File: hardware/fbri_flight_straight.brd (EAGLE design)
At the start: 12 x 55 mm, 38 parts, among them U1 SAM_D20E, U2 SI4060, U3 MAX1947, U4 ANTENOVA_GPS_M10382, U5 S25FS-S

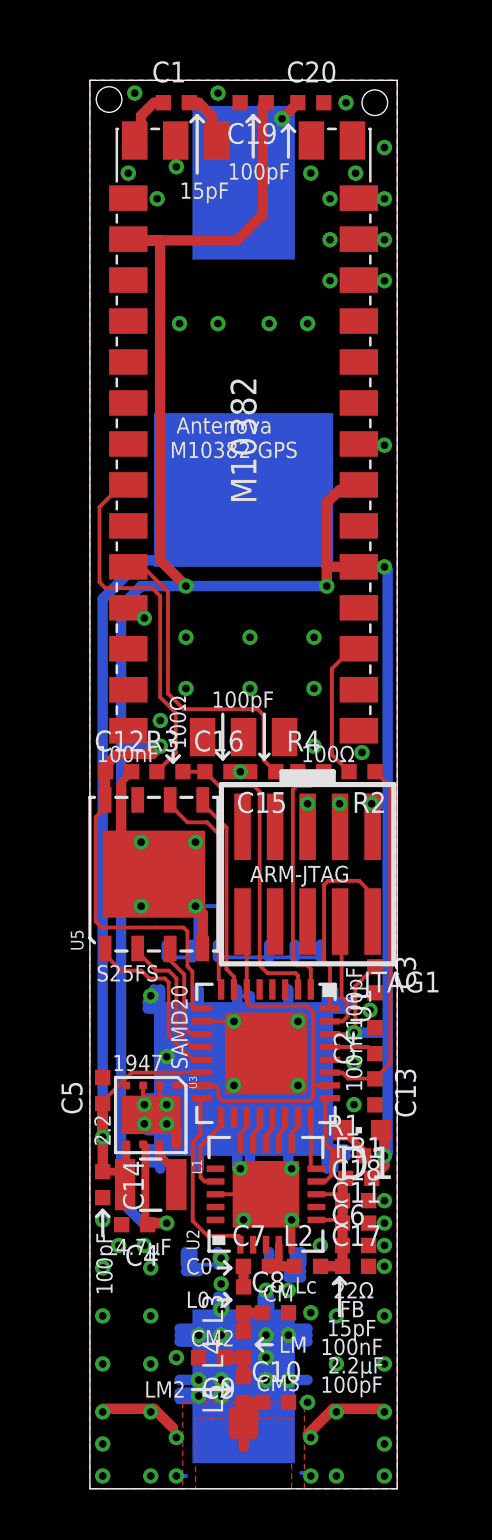
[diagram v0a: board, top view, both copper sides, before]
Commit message: Nearly there, about to re-work MAX1947
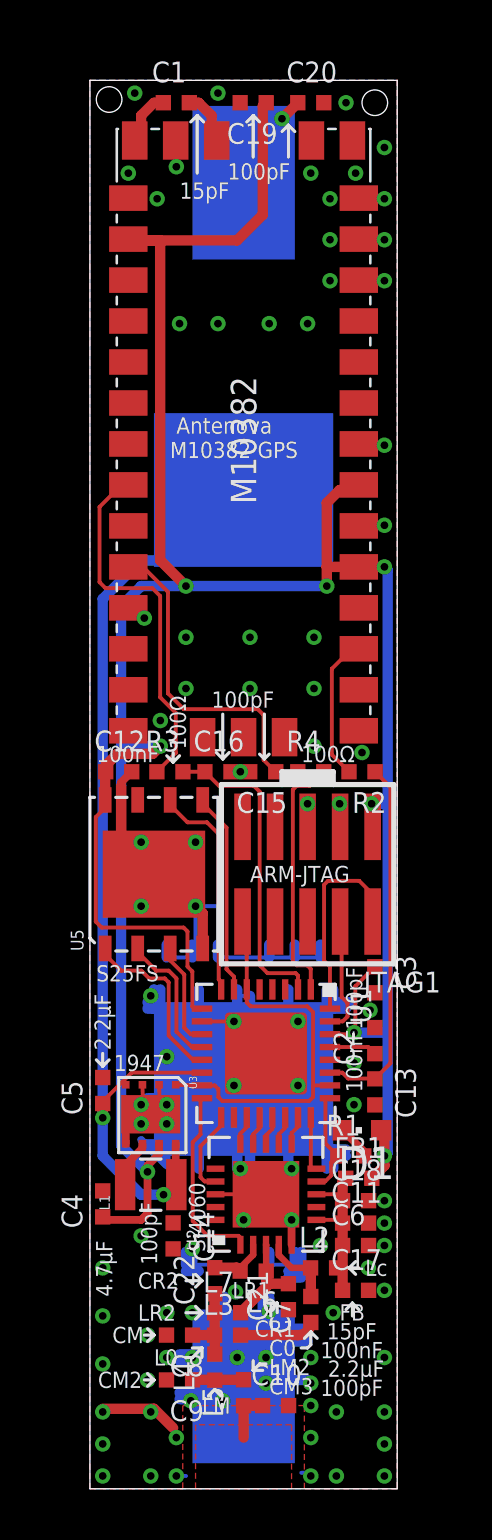
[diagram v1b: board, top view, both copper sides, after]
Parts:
- added C21: 15pF, microbuilder_v3:_0402
- added C22, L6, L7: DNP, microbuilder_v3:_0402
- moved C8 3.85 mm to (3.50, 6.00), turned to 180 degrees
- moved C14 3.40 mm to (3.25, 9.88)
- moved C7 2.71 mm to (8.62, 7.00), turned to 90 degrees
- moved C9 1.53 mm to (3.50, 4.25)
- moved L3 1.51 mm to (5.38, 6.00), turned to 0 degrees
- moved C4 1.49 mm to (0.50, 11.1), turned to 90 degrees
- moved L4 1.43 mm to (4.88, 4.75)
- moved C17 0.94 mm to (10.4, 7.75)
- moved L2 0.63 mm to (9.12, 8.62)
- moved C10 0.12 mm to (7.25, 3.25)
- moved L5 0.12 mm to (6.00, 3.75)
- turned L1 to 90 degrees
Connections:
- new net RXN: C21.2, L6.1, L7.2, U2.3
- new net RXP: C22.2, L6.2, U2.2
- net 1.2V: now also U3.8; no longer U3.5
- net 1.8V: now also U3.7; no longer U3.6
- net FILTER1: now also C22.1, L7.1
- net GND: now also C21.1, U3.5; no longer U3.8
- net LX: now also U3.6; no longer U3.7
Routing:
- net RXN: track 0.00 -> 3.99 mm
- net GND: track 89.5 -> 86.0 mm, vias 105 -> 98
- net ANT: track 5.04 -> 2.35 mm
- net RXP: track 0.00 -> 2.42 mm
- net 1.8V: track 120.6 -> 118.4 mm
- net TANK: track 0.82 -> 2.95 mm
- net FILTER1: track 1.48 -> 3.23 mm
- net 1.2V: track 38.9 -> 39.9 mm, vias 1 -> 2
- net FILTER2: track 1.48 -> 2.01 mm
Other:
- board text added: "CR1"
- board text added: "CR2"
- board text added: "FB 15pF 100nF 100pF"
- board text added: "LR1"
- board text added: "LR2"
- board text added: "Si4060"
- board text removed: "2.2"
- board text removed: "22Ω FB 15pF 100nF 100pF"
- board text removed: "SAMD20"

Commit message: Before rename
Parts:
- removed C4: 4.7µF, microbuilder_v3:_0402
- added C23: 4.7µF, resistor:C0603K
- moved C14 8.55 mm to (1.00, 18.1), turned to 0 degrees
- moved L1 4.07 mm to (1.62, 15.9), turned to 270 degrees
- moved C5 3.48 mm to (1.00, 19.0), turned to 0 degrees
- moved U3 3.14 mm to (1.44, 11.6), turned to 90 degrees
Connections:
- net 1.8V: now also C23.1; no longer C4.1
- net GND: now also C23.2; no longer C4.2
- net RESETN: now also U1.16; no longer U1.15
- net SI_HF_CLK: now also U1.18; no longer U1.17
- net SI_SDN: now also U1.17; no longer U1.16
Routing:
- net RESETN: track 15.8 -> 24.5 mm
- net 1.2V: track 39.9 -> 45.8 mm
- net 1.8V: track 118.4 -> 113.0 mm
- net GND: track 86.0 -> 83.6 mm, vias 98 -> 99
- net LX: track 1.88 -> 3.46 mm
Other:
- board text added: "3.3µH"
- board text removed: "S25FS"
